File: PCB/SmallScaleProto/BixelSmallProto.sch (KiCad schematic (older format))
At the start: 25 parts

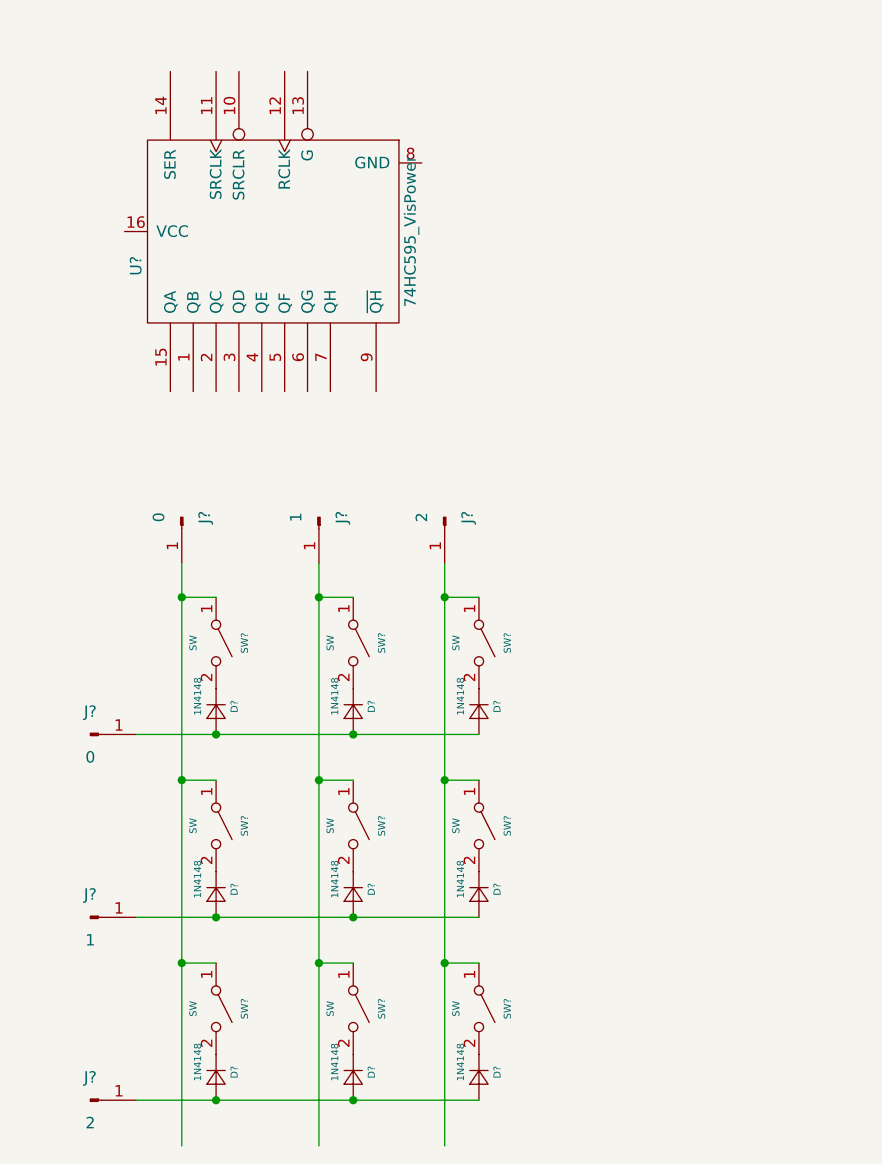
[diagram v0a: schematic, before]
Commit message: adding chained 595 example
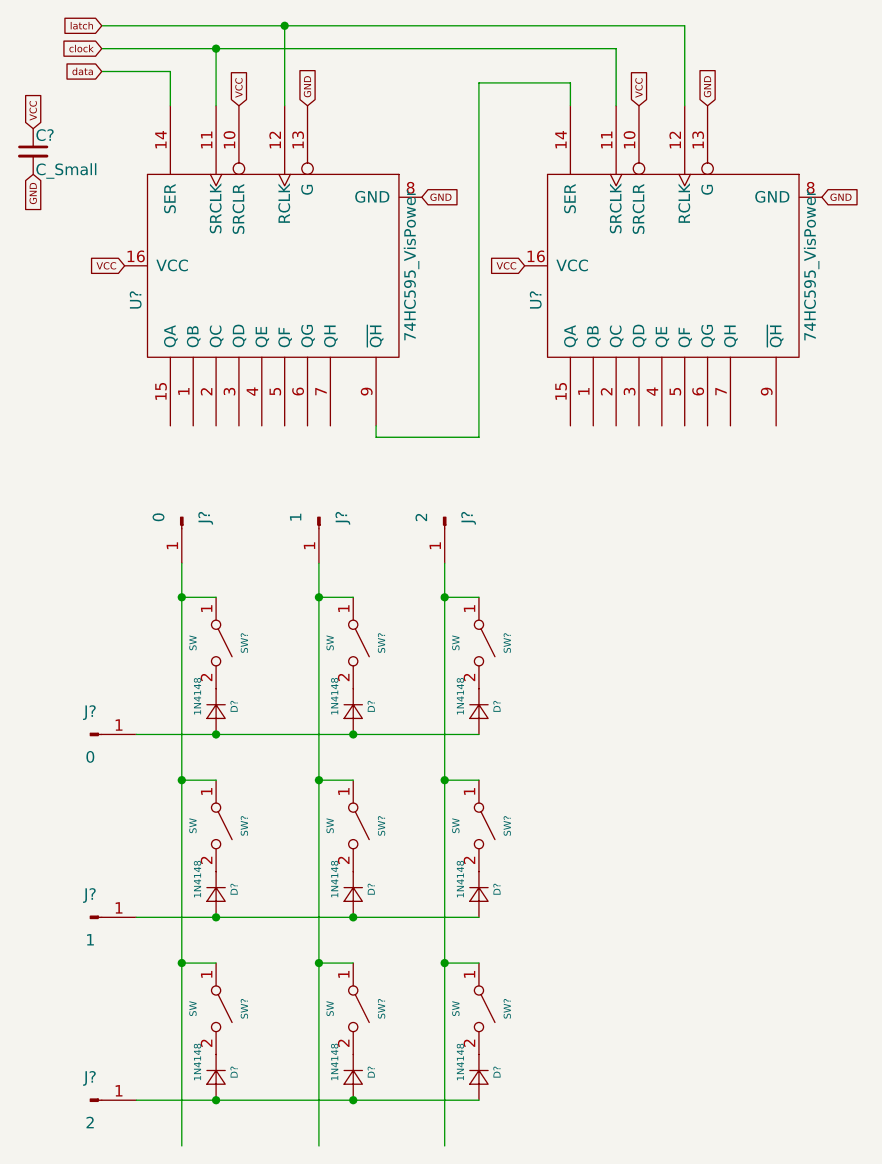
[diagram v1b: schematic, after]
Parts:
- added C?: C_Small, symbol C_Small
- added U?: 74HC595_VisPower, symbol 74HC595_VisPower
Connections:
- net labels added: GND, VCC, clock, data, latch
- wire segments 15 -> 28
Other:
- moved on the sheet: U?
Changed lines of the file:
@@
 LIBS:valves
 LIBS:74hc595_VisPower
+LIBS:BixelSmallProto-cache
 EELAYER 25 0
 EELAYER END
@@
 L 74HC595_VisPower U?
 U 1 1 5B11EA08
-P 2200 1550
-F 0 "U?" H 2350 2150 50  0000 C CNN
-F 1 "74HC595_VisPower" H 2200 950 50  0000 C CNN
-F 2 "" H 2200 1550 50  0001 C CNN
-F 3 "" H 2200 1550 50  0001 C CNN
-	1    2200 1550
+P 2200 1700
+F 0 "U?" H 2350 2300 50  0000 C CNN
+F 1 "74HC595_VisPower" H 2200 1100 50  0000 C CNN
+F 2 "" H 2200 1700 50  0001 C CNN
+F 3 "" H 2200 1700 50  0001 C CNN
+	1    2200 1700
 	0    -1   1    0
 $EndComp
@@
 	0    1    1    0
 $EndComp
+Text GLabel 1450 850  0    31   Input ~ 0
+data
+Text GLabel 1450 650  0    31   Input ~ 0
+latch
+Text GLabel 1450 750  0    31   Input ~ 0
+clock
+Text GLabel 2350 1000 1    31   Input ~ 0
+GND
+Text GLabel 2850 1400 2    31   Input ~ 0
+GND
+Text GLabel 2050 1000 1    31   Input ~ 0
+VCC
+Text GLabel 1550 1700 0    31   Input ~ 0
+VCC
+Text GLabel 1150 1100 1    31   Input ~ 0
+VCC
+Text GLabel 1150 1300 3    31   Input ~ 0
+GND
+$Comp
+L C_Small C?
+U 1 1 5B490C73
+P 1150 1200
+F 0 "C?" H 1160 1270 50  0000 L CNN
+F 1 "C_Small" H 1160 1120 50  0000 L CNN
+F 2 "" H 1150 1200 50  0001 C CNN
+F 3 "" H 1150 1200 50  0001 C CNN
+	1    1150 1200
+	1    0    0    -1
+$EndComp
+$Comp
+L 74HC595_VisPower U?
+U 1 1 5B491397
+P 3950 1700
+F 0 "U?" H 4100 2300 50  0000 C CNN
+F 1 "74HC595_VisPower" H 3950 1100 50  0000 C CNN
+F 2 "" H 3950 1700 50  0001 C CNN
+F 3 "" H 3950 1700 50  0001 C CNN
+	1    3950 1700
+	0    -1   1    0
+$EndComp
+Text GLabel 4100 1000 1    31   Input ~ 0
+GND
+Text GLabel 4600 1400 2    31   Input ~ 0
+GND
+Text GLabel 3800 1000 1    31   Input ~ 0
+VCC
+Text GLabel 3300 1700 0    31   Input ~ 0
+VCC
+Wire Wire Line
+	2650 2400 2650 2450
+Wire Wire Line
+	2650 2450 3100 2450
+Wire Wire Line
+	3100 2450 3100 900
+Wire Wire Line
+	3100 900  3500 900
+Wire Wire Line
+	3500 900  3500 1000
+Wire Wire Line
+	1450 850  1750 850
+Wire Wire Line
+	1750 850  1750 1000
+Wire Wire Line
+	1450 750  3700 750
+Wire Wire Line
+	1950 750  1950 1000
+Wire Wire Line
+	1450 650  4000 650
+Wire Wire Line
+	2250 650  2250 1000
+Wire Wire Line
+	3700 750  3700 1000
+Connection ~ 1950 750
+Wire Wire Line
+	4000 650  4000 1000
+Connection ~ 2250 650
 $EndSCHEMATC
